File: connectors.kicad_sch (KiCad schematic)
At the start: 17 parts, among them J501 Conn_WS2812_Extern, T501 AO3400A, T502 AO3400A, X501 BH-00105, X502 USB3.1C16PFSMT, X503 USB3.1C16PFSMT, X504 S4B-PH-SM4-K-TB(LF)(SN), X505 PJ-327C-4A, X506 PJ-327C-4A, X507 KF2EDGR-3.81-3P

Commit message: start rework of baseboard.
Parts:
- renumbered D501 to D17, D502 to D18, J501 to J2, JP501 to JP1, R501 to R49, R502 to R50, R503 to R51, R504 to R52, T501 to T7, T502 to T8, X504 to X10, X505 to X11, X506 to X12, X507 to X13, X501 to X7, X502 to X8, X503 to X9

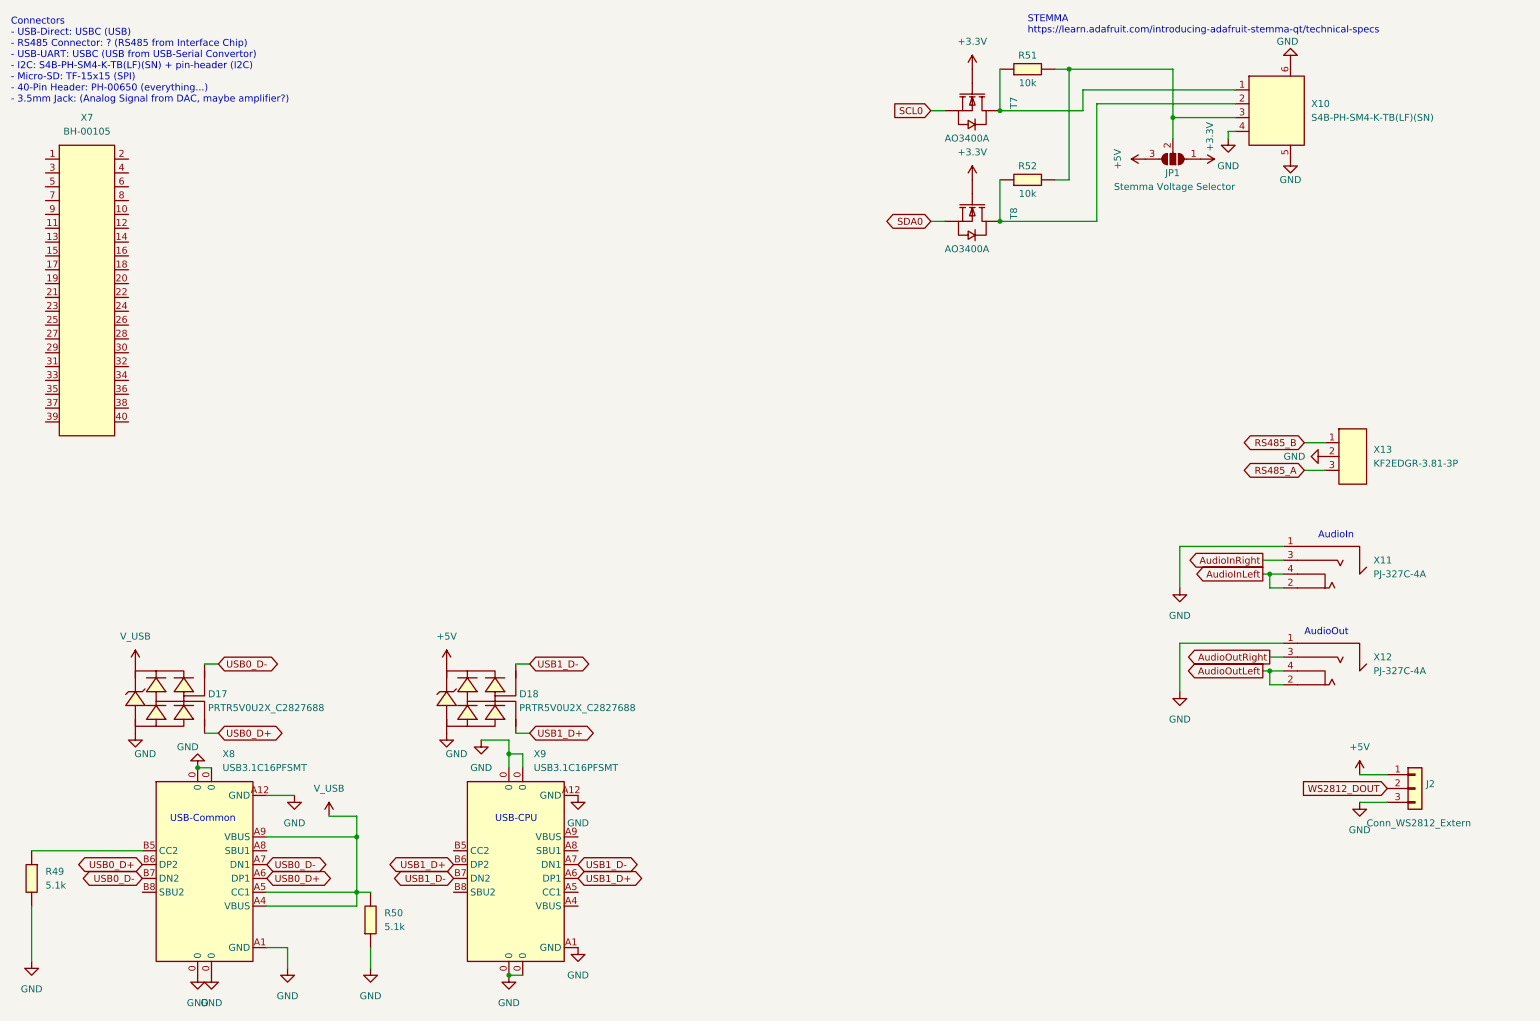
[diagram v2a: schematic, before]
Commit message: rework schematic. remove unnescessary stuff. Connect PCIE Connector. Select new Temperature Sensor (I2C) Define Signals for 40Pin Connector
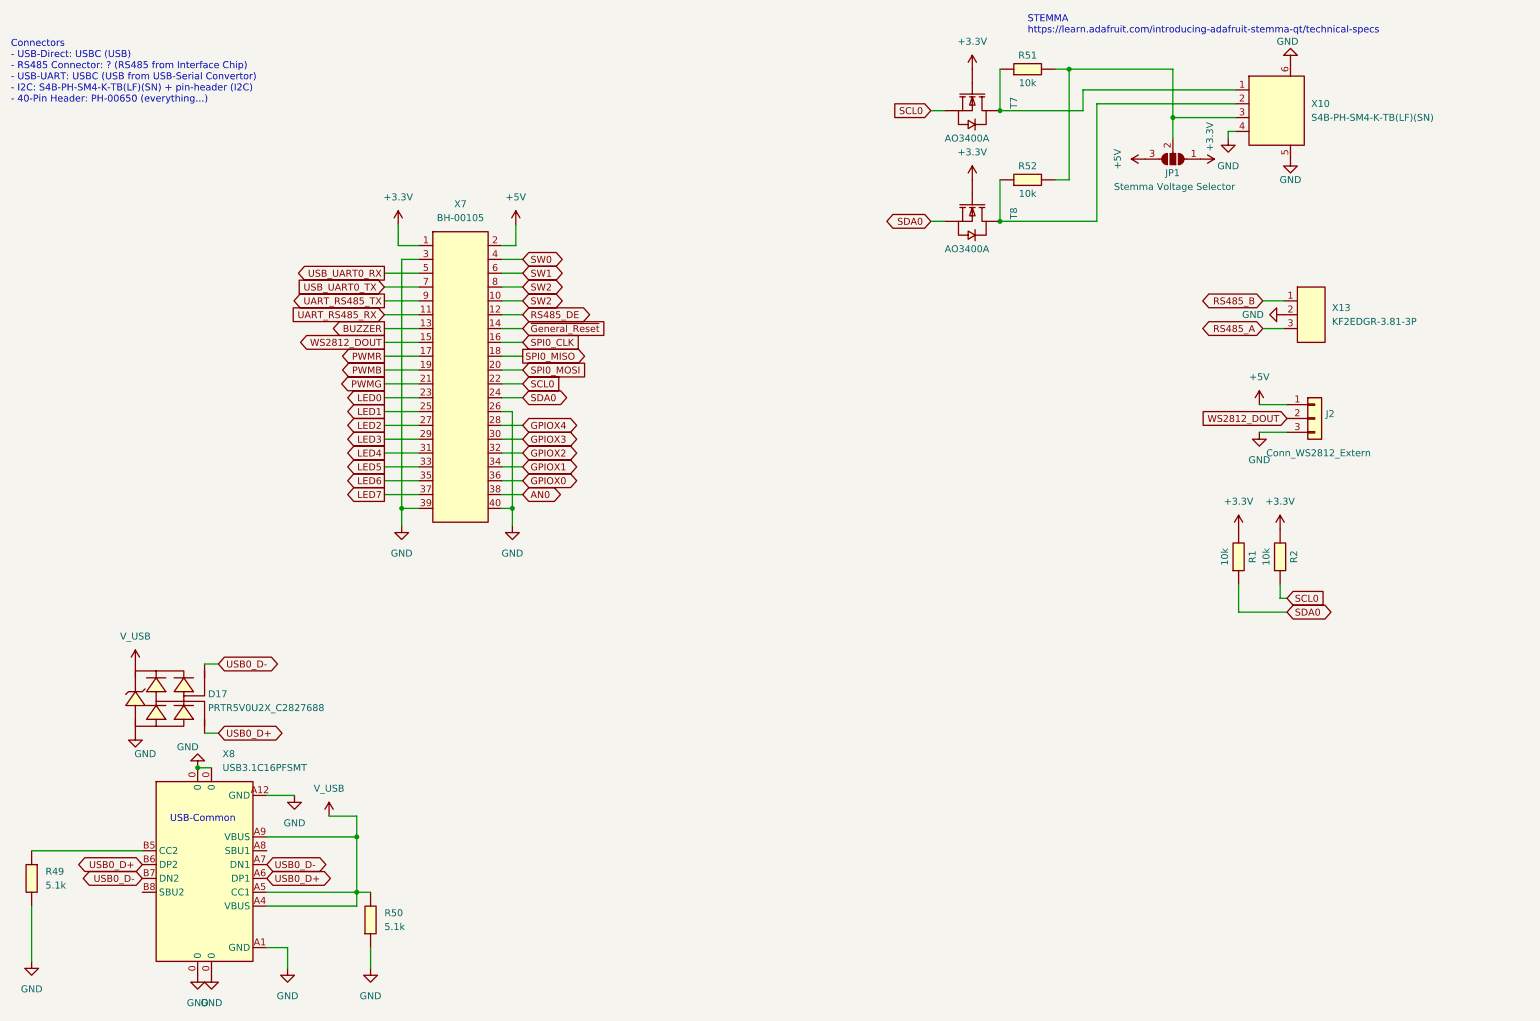
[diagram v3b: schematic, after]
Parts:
- removed D18: PRTR5V0U2X_C2827688, SOT-143-4_L2.9-W1.3-P1.92-LS2.4-BL, symbol eduboardv2:PRTR5V0U2X_C2827688
- removed X11, X12: PJ-327C-4A, eduboardv2:AUDIO-SMD_PJ-327C-4A, symbol eduboardv2:PJ-327C-4A
- removed X9: USB3.1C16PFSMT, eduboardv2:USB-C-SMD_TYPE-C-USB-17, symbol eduboardv2:USB3.1C16PFSMT
- added R1, R2: 10k, eduboardv2:R0402, symbol eduboardv2:0402WGF100JTCE
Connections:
- net +3.3V: now also X7.1, R1.2, R2.2
- net +5V: now also X7.2
- net GND: now also X7.26, X7.3, X7.39, X7.40
- net SCL0: now also X7.22, R2.1
- net SDA0: now also X7.24, R1.1
- net WS2812_DOUT: now also X7.15
- net SW2: now reaches X7.10
- net SW2: now also X7.8
- net UART_RS485_RX: now reaches X7.11
- net RS485_DE: now reaches X7.12
- net BUZZER: now reaches X7.13
- net ~{General_Reset}: now reaches X7.14
- net SPI0_CLK: now reaches X7.16
- net PWMR: now reaches X7.17
- net SPI0_MISO: now reaches X7.18
- net PWMB: now reaches X7.19
- net SPI0_MOSI: now reaches X7.20
- net PWMG: now reaches X7.21
- net LED0: now reaches X7.23
- net LED1: now reaches X7.25
- net LED2: now reaches X7.27
- net GPIOX4: now reaches X7.28
- net LED3: now reaches X7.29
- net GPIOX3: now reaches X7.30
- net LED4: now reaches X7.31
- net GPIOX2: now reaches X7.32
- net LED5: now reaches X7.33
- net GPIOX1: now reaches X7.34
- net LED6: now reaches X7.35
- net GPIOX0: now reaches X7.36
- net LED7: now reaches X7.37
- net AN0: now reaches X7.38
- net SW0: now reaches X7.4
- net USB_UART0_RX: now reaches X7.5
- net SW1: now reaches X7.6
- net USB_UART0_TX: now reaches X7.7
- net UART_RS485_TX: now reaches X7.9
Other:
- note added: "Connectors - USB-Direct: USBC (USB) - RS485 Connector: ? (RS485 from Interface Chip) - USB-UART: USBC (USB from USB-Serial Convertor) - I2C: S4B-PH-SM4-K-TB(LF)(SN) + pin-header (I2C) - 40-Pin Header: PH-00650 (everything...)"
- note removed: "AudioIn"
- note removed: "AudioOut"
- note removed: "Connectors - USB-Direct: USBC (USB) - RS485 Connector: ? (RS485 from Interface Chip) - USB-UART: USBC (USB from USB-Serial Convertor) - I2C: S4B-PH-SM4-K-TB(LF)(SN) + pin-header (I2C) - Micro-SD: TF-15x15 (SPI) - 40-Pin Header: PH-00650 (everything...) - 3.5mm Jack: (Analog Signal from DAC, maybe amplifier?)"
- note removed: "USB-CPU"
- moved on the sheet: J2, X13, X7

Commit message: replace display with better module, start layout parts on pcb.
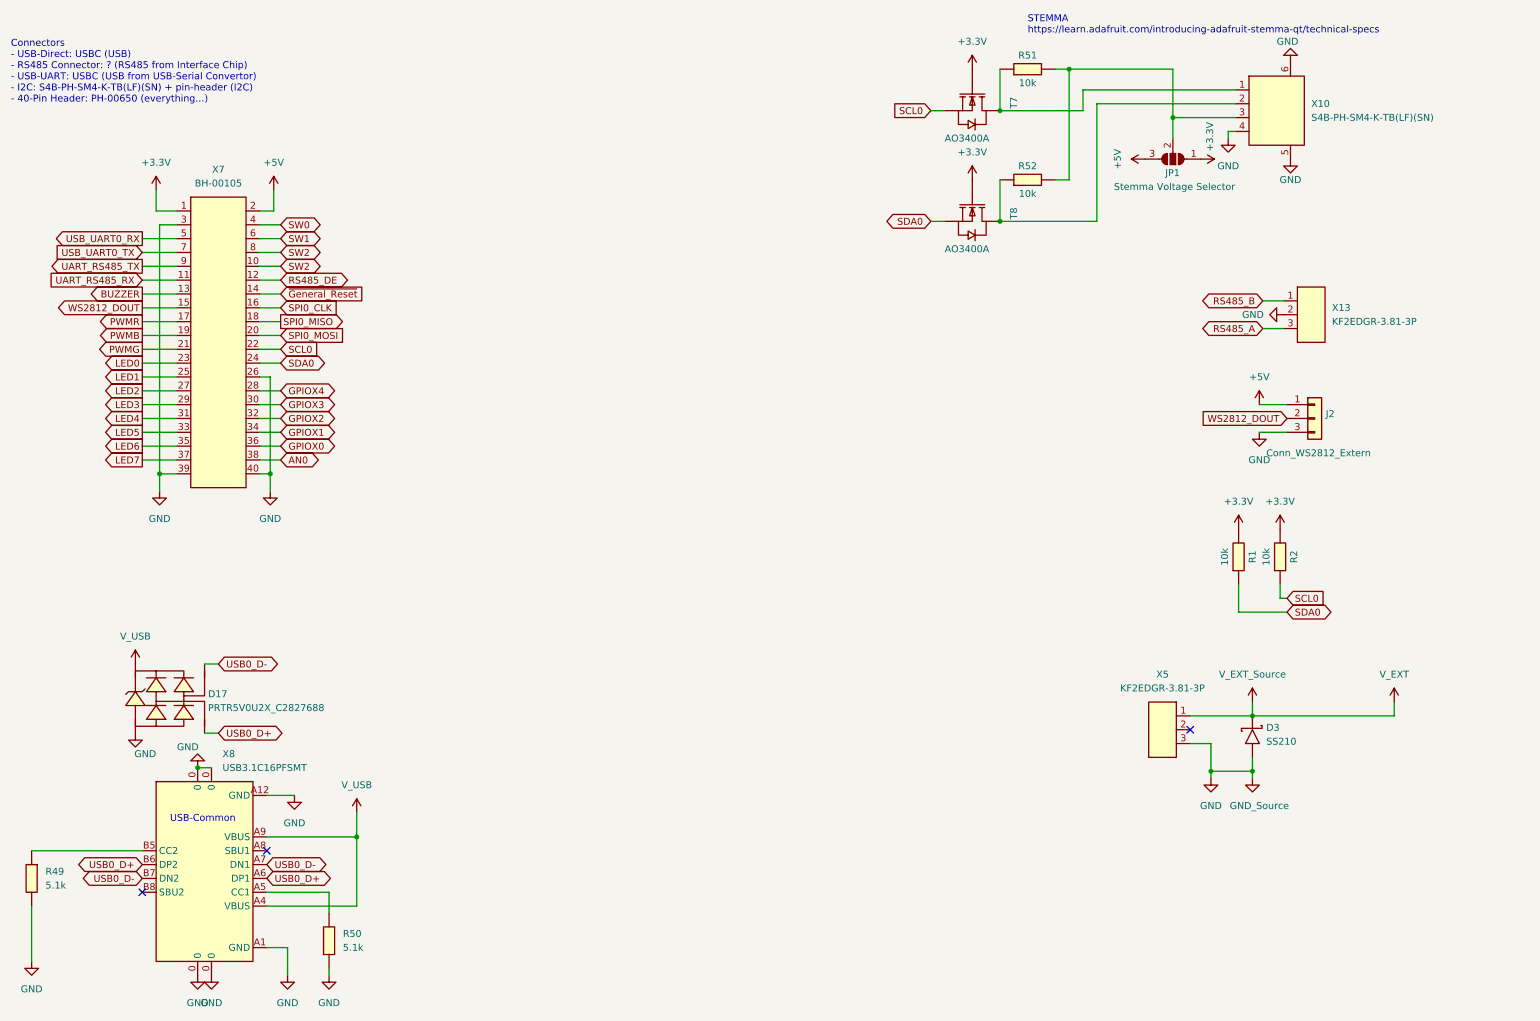
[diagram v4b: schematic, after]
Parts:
- added D3: SS210, EduboardV2_kicadlib:SMA_L4.3-W2.6-LS5.2-RD, symbol eduboardv2:SS210
- added X5: KF2EDGR-3.81-3P, EduboardV2_kicadlib:CONN-TH_3P-P3.81_KF2EDGR-3.81-3P, symbol eduboardv2:KF2EDGR-3.81-3P
- D17: footprint SOT-143-4_L2.9-W1.3-P1.92-LS2.4-BL -> EduboardV2_kicadlib:SOT-143-4_L2.9-W1.3-P1.92-LS2.4-BL
- R1, R2, R49, R50, R51, R52: footprint eduboardv2:R0402 -> Resistor_SMD:R_0402_1005Metric_Pad0.72x0.64mm_HandSolder
- T7, T8: footprint eduboardv2:SOT-23-3_L2.9-W1.6-P1.90-LS2.8-BR -> EduboardV2_kicadlib:SOT-23-3_L2.9-W1.6-P1.90-LS2.8-BR
- X10: footprint eduboardv2:CONN-SMD_S4B-PH-SM4-K-TB-LF-SN -> EduboardV2_kicadlib:CONN-SMD_S4B-PH-SM4-K-TB-LF-SN
- X13: footprint eduboardv2:CONN-TH_3P-P3.81_KF2EDGR-3.81-3P -> EduboardV2_kicadlib:CONN-TH_3P-P3.81_KF2EDGR-3.81-3P
- X7: footprint eduboardv2:IDC-SMD_BH-00105 -> EduboardV2_kicadlib:IDC-SMD_BH-00105
- X8: footprint eduboardv2:USB-C-SMD_TYPE-C-USB-17 -> EduboardV2_kicadlib:USB-C-SMD_TYPE-C-USB-17
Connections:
- net GND: now also D3.2 (A), X5.3
- net V_USB: no longer R50.2, X8.A5 (CC1)
- new net: R50.2, X8.A5 (CC1)
- new net V_EXT: D3.1 (K), X5.1
- no-connect marks 0 -> 3
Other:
- moved on the sheet: R50, X7

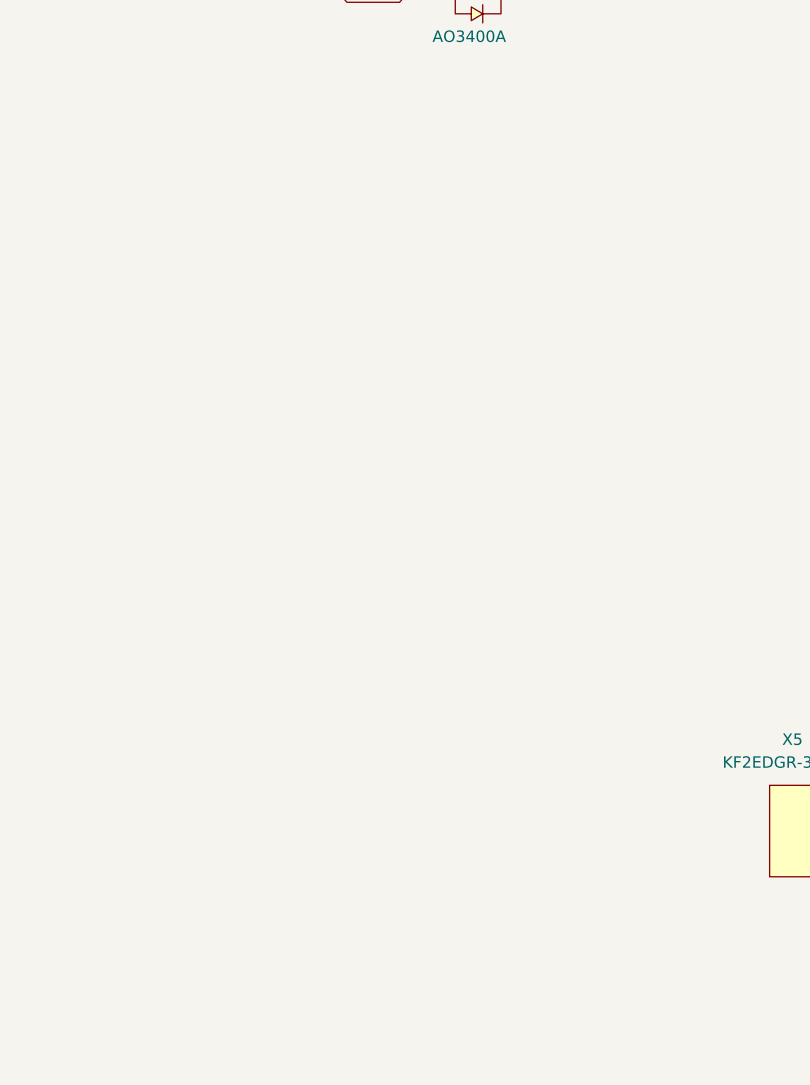
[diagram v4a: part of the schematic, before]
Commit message: add protoboard area. not yet done
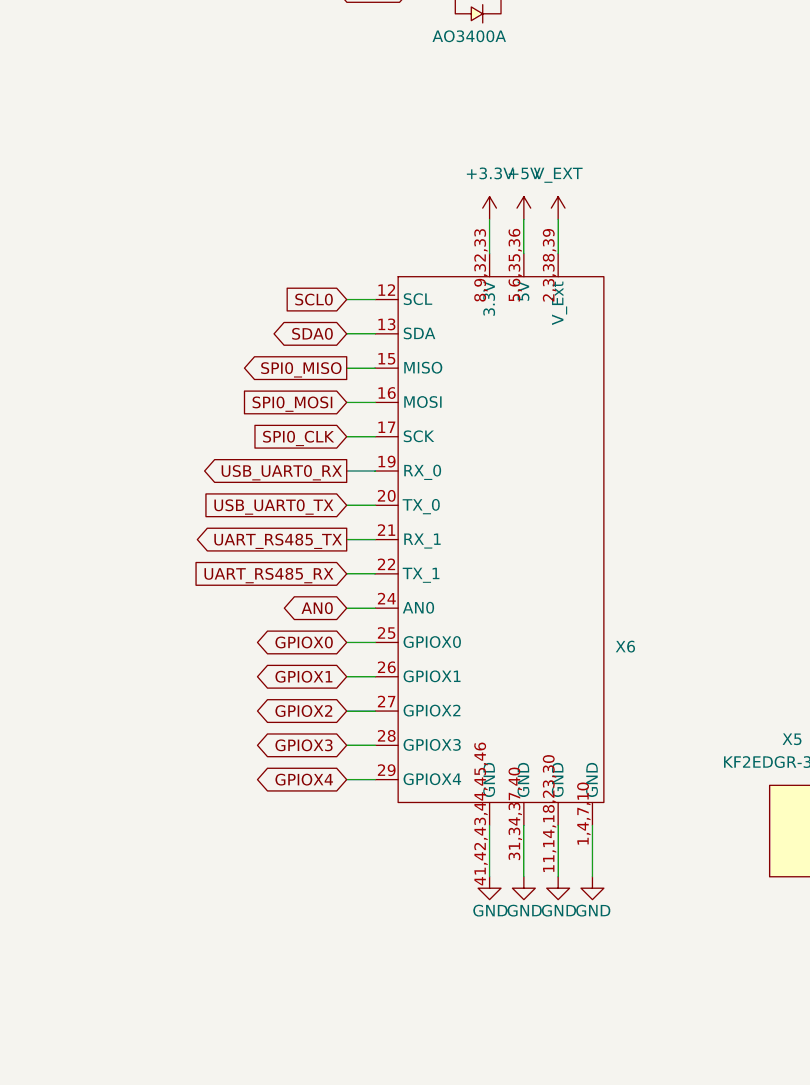
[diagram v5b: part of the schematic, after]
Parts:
- added X6: ~, EduboardV2_kicadlib:protoboard_patch, symbol EduboardV2_kicadlib:protoboard_patch
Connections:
- net +3.3V: now also X6.8,9,32,33 (3.3V)
- net +5V: now also X6.5,6,35,36 (5V)
- net AN0: now also X6.24 (AN0)
- net GND: now also X6.1,4,7,10 (GND), X6.11,14,18,23,30 (GND), X6.31,34,37,40 (GND), X6.41,42,43,44,45,46 (GND)
- net GPIOX0: now also X6.25 (GPIOX0)
- net GPIOX1: now also X6.26 (GPIOX1)
- net GPIOX2: now also X6.27 (GPIOX2)
- net GPIOX3: now also X6.28 (GPIOX3)
- net GPIOX4: now also X6.29 (GPIOX4)
- net SCL0: now also X6.12 (SCL)
- net SDA0: now also X6.13 (SDA)
- net SPI0_CLK: now also X6.17 (SCK)
- net SPI0_MISO: now also X6.15 (MISO)
- net SPI0_MOSI: now also X6.16 (MOSI)
- net UART_RS485_RX: now also X6.22 (TX_1)
- net UART_RS485_TX: now also X6.21 (RX_1)
- net USB_UART0_RX: now also X6.19 (RX_0)
- net USB_UART0_TX: now also X6.20 (TX_0)
- net V_EXT: now also X6.2,3,38,39 (V_Ext)
